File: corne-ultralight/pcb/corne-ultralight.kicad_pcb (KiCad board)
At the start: 2 copper layers, 275.5 x 105.6 mm, 148 parts, among them J2 OLED, J5 Breakaway_Tabs, J7 OLED, SW1 SW_PUSH, SW10 SW_PUSH, SW11 SW_PUSH, SW12 SW_PUSH, SW13 SW_PUSH, SW14 SW_PUSH, SW15 SW_PUSH, SW16 SW_PUSH, SW17 SW_PUSH, SW18 SW_PUSH, SW19 SW_PUSH, SW2 SW_PUSH, SW20 SW_PUSH, SW21 SW_PUSH, SW22 SW_PUSH, SW23 SW_PUSH, SW24 SW_PUSH, SW25 SW_PUSH, SW26 SW_PUSH, SW27 SW_PUSH, SW28 SW_PUSH, SW29 SW_PUSH, SW3 SW_PUSH, SW30 SW_PUSH, SW31 SW_PUSH, SW32 SW_PUSH, SW33 SW_PUSH, SW34 SW_PUSH, SW35 SW_PUSH, SW36 SW_PUSH, SW37 SW_PUSH, SW38 SW_PUSH, SW39 SW_PUSH, SW4 SW_PUSH, SW40 SW_PUSH, SW41 SW_PUSH, SW42 SW_PUSH, SW5 SW_PUSH, SW6 SW_PUSH, SW7 SW_PUSH, SW8 SW_PUSH, SW9 SW_PUSH, U1 ProMicro, U2 ProMicro

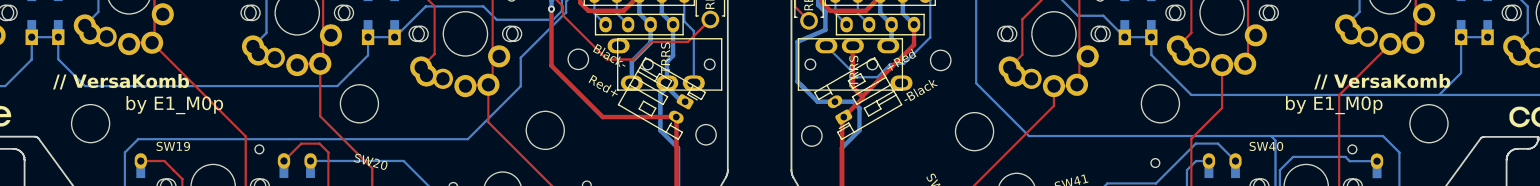
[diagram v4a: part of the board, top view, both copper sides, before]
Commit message: Logo relocated
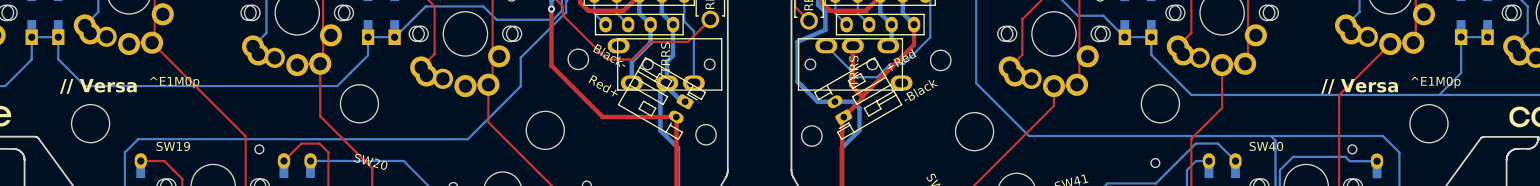
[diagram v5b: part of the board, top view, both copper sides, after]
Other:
- board text added: "// Versa"
- board text added: "^E1M0p"
- board text removed: "// VersaKomb"
- board text removed: "by E1_M0p"
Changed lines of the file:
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@@
 		(layer "Edge.Cuts")
 	)
+	(gr_text "^E1M0p"
+		(at 77.2125 86.945 -0)
+		(layer "B.SilkS")
+		(effects
+			(font
+				(size 1 1)
+				(thickness 0.125)
+			)
+			(justify left mirror)
+		)
+	)
+	(gr_text "^E1M0p"
+		(at 219.484848 86.945 -0)
+		(layer "B.SilkS")
+		(effects
+			(font
+				(size 1 1)
+				(thickness 0.125)
+			)
+			(justify left mirror)
+		)
+	)
 	(gr_text "-Black"
 		(at 141.7125 89.57 -30)
@@
 		)
 	)
+	(gr_text "// Versa"
+		(at 87.216071 87.445 -0)
+		(layer "B.SilkS")
+		(effects
+			(font
+				(size 1.5 1.5)
+				(thickness 0.3)
+				(bold yes)
+			)
+			(justify left mirror)
+		)
+	)
 	(gr_text "ON"
 		(at 141.8525 38.045 180)
@@
 		)
 	)
-	(gr_text "// VersaKomb"
-		(at 87.546428 86.945 -0)
-		(layer "B.SilkS")
-		(effects
-			(font
-				(size 1.5 1.5)
-				(thickness 0.3)
-				(bold yes)
-			)
-			(justify left mirror)
-		)
-	)
 	(gr_text "OFF"
 		(at 168.8525 38.045 180)
@@
 		)
 	)
-	(gr_text "-Black"
-		(at 138.7125 64.945 90)
+	(gr_text "// Versa"
+		(at 229.488419 87.445 -0)
 		(layer "B.SilkS")
 		(effects
 			(font
-				(size 1 1)
-				(thickness 0.15)
+				(size 1.5 1.5)
+				(thickness 0.3)
+				(bold yes)
 			)
 			(justify left mirror)
 		)
 	)
-	(gr_text "by E1_M0p"
-		(at 222.2125 89.445 -0)
+	(gr_text "-Black"
+		(at 138.7125 64.945 90)
 		(layer "B.SilkS")
 		(effects
 			(font
-				(size 1.5 1.5)
-				(thickness 0.1875)
+				(size 1 1)
+				(thickness 0.15)
 			)
 			(justify left mirror)
@@
 		)
 	)
-	(gr_text "// VersaKomb"
-		(at 230.497296 86.945 -0)
-		(layer "B.SilkS")
-		(effects
-			(font
-				(size 1.5 1.5)
-				(thickness 0.3)
-				(bold yes)
-			)
-			(justify left mirror)
-		)
-	)
-	(gr_text "by E1_M0p"
-		(at 90.7125 89.445 -0)
-		(layer "B.SilkS")
-		(effects
-			(font
-				(size 1.5 1.5)
-				(thickness 0.1875)
-			)
-			(justify left mirror)
-		)
-	)
 	(gr_text "Corne Ultralight v2.0 PCB Designed by foostan, mods by petejohanson"
 		(at 191.7125 68.56 0)
@@
 		)
 	)
+	(gr_text "^E1M0p"
+		(at 223.884847 86.945 0)
+		(layer "F.SilkS")
+		(effects
+			(font
+				(size 1 1)
+				(thickness 0.125)
+			)
+			(justify left)
+		)
+	)
 	(gr_text "OFF"
 		(at 171.7125 37.795 180)
@@
 		)
 	)
+	(gr_text "// Versa"
+		(at 213.881276 87.445 0)
+		(layer "F.SilkS")
+		(effects
+			(font
+				(size 1.5 1.5)
+				(thickness 0.3)
+				(bold yes)
+			)
+			(justify left)
+		)
+	)
 	(gr_text "+Red"
 		(at 135.83 59.445 -90)
@@
 		)
 	)
-	(gr_text "// VersaKomb"
-		(at 70.601786 86.945 0)
+	(gr_text "// Versa"
+		(at 71.383929 87.445 0)
 		(layer "F.SilkS")
 		(effects
@@
 		)
 	)
-	(gr_text "by E1_M0p"
-		(at 78.7125 89.445 0)
+	(gr_text "^E1M0p"
+		(at 81.3875 86.945 0)
 		(layer "F.SilkS")
 		(effects
 			(font
-				(size 1.5 1.5)
-				(thickness 0.1875)
+				(size 1 1)
+				(thickness 0.125)
 			)
 			(justify left)
@@
 		)
 	)
-	(gr_text "// VersaKomb"
-		(at 213.099133 86.945 0)
-		(layer "F.SilkS")
-		(effects
-			(font
-				(size 1.5 1.5)
-				(thickness 0.3)
-				(bold yes)
-			)
-			(justify left)
-		)
-	)
 	(gr_text "+Red"
 		(at 170.7125 116.945 30)
@@
 		)
 	)
-	(gr_text "by E1_M0p"
-		(at 209.7125 89.445 0)
-		(layer "F.SilkS")
-		(effects
-			(font
-				(size 1.5 1.5)
-				(thickness 0.1875)
-			)
-			(justify left)
-		)
-	)
 	(gr_text "-Black"
 		(at 169.7125 114.945 30)
@@
 	)
 	(group ""
+		(members "0ffdac26-deab-4092-bf70-1deacd5aef2e" "998406bc-4587-4f5e-a01f-56acd46aa053")
+	)
+	(group ""
+		(members "0d20a1ce-ac43-4072-a8c1-6ed2a3d40657" "204c0979-0e7f-4b7e-9039-b8af16723e6c")
+	)
+	(group ""
 		(members "2187ae59-cf06-4ae2-91b6-236c0a0f70c2" "6999038d-f6d8-4e0f-9d20-872c00953e82"
 			"963028a2-7672-429f-a7cc-4c051f91424c" "9814480d-787a-496e-99a7-91b93430a16f"
@@
 	)
 	(group ""
+		(members "55fb019d-3973-4d45-8622-56472f458ae5" "95f94ae2-a65c-44bb-b344-aae6a263121a")
+	)
+	(group ""
 		(members "013f1f25-df12-4825-a242-8f30f3cd3b16" "5f772bcf-fc59-4ca1-a4e6-d1eedcd91c5c")
 	)
@@
 	)
 	(group ""
+		(members "1c0b1fae-bb3e-4696-8439-dd348b1b6155" "2835c844-1c04-458d-9ca5-06f73f505be4")
+	)
+	(group ""

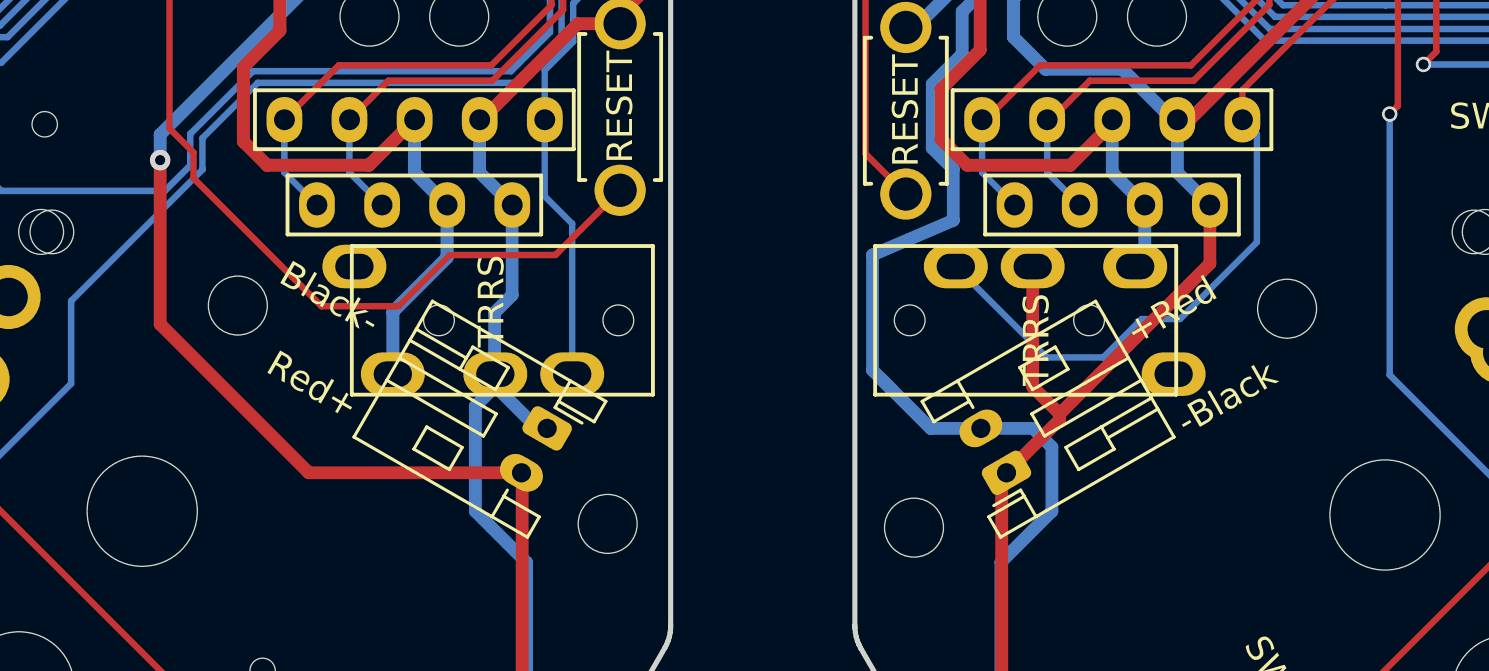
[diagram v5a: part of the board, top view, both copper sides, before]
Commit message: Two small cable holes at the bottom edge of the visor
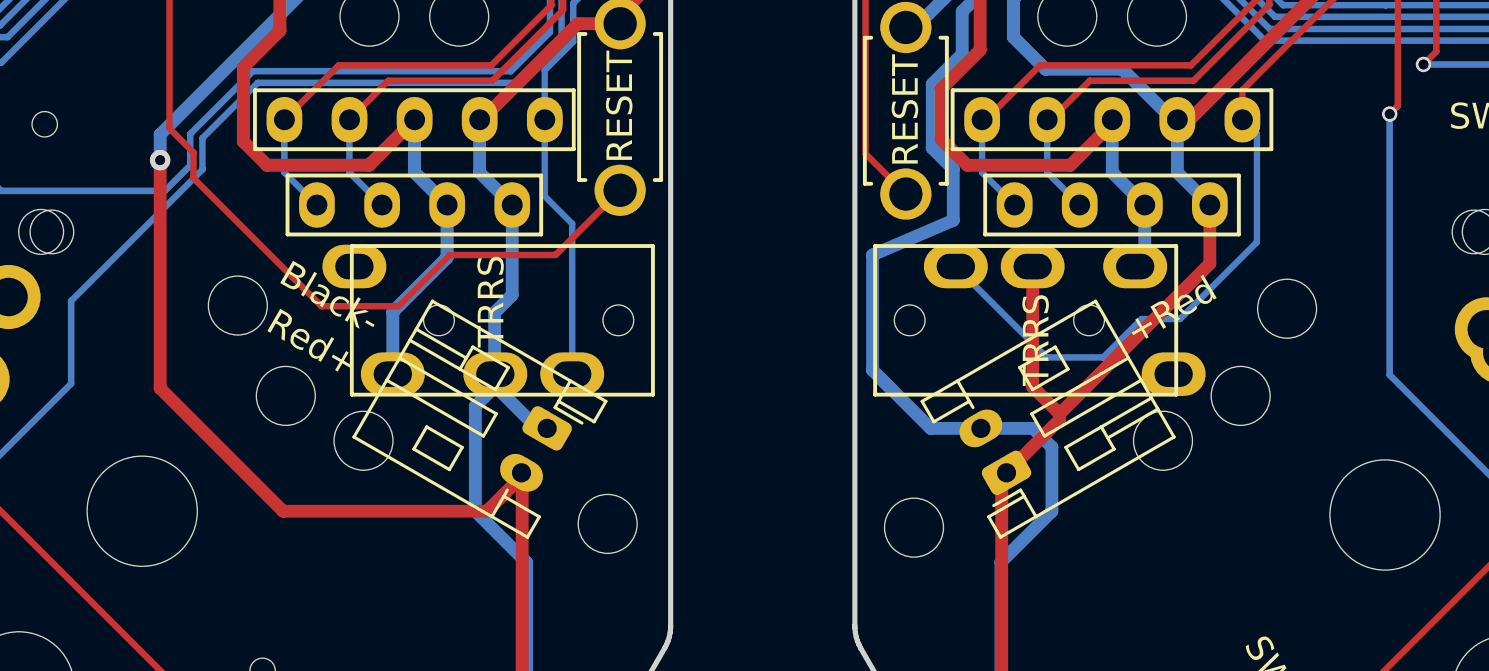
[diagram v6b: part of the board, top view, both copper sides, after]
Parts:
- added Ref**: Val**, kbd:thread_m2, F.Cu at (131.8, 87.9)
- added Ref**: Val**, kbd:thread_m2, F.Cu at (134.8, 89.7)
- added Ref**: Val**, kbd:thread_m2, F.Cu at (166.0, 89.7)
- added Ref**: Val**, kbd:thread_m2, F.Cu at (169.1, 87.9)
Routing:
- net Net-(BATJ1-Pin_2): track 97.3 -> 99.9 mm

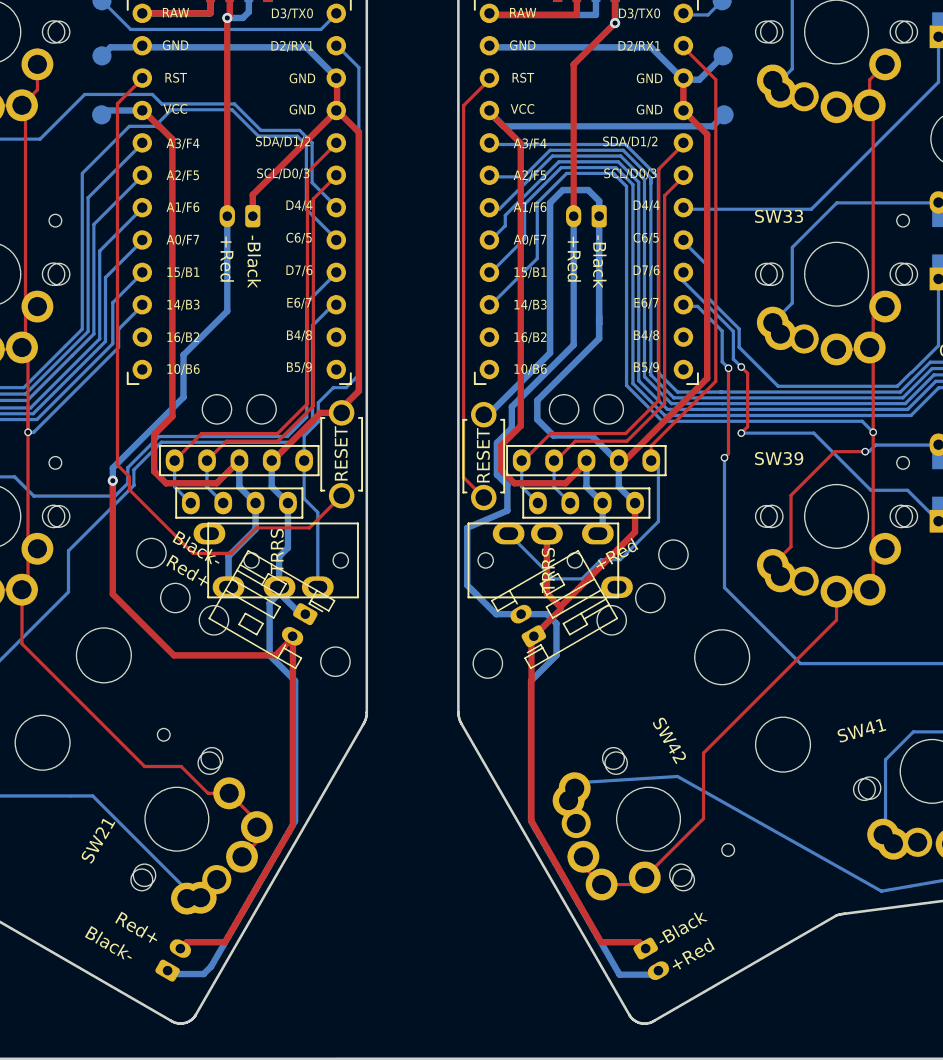
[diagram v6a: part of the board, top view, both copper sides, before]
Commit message: Improved cable holes
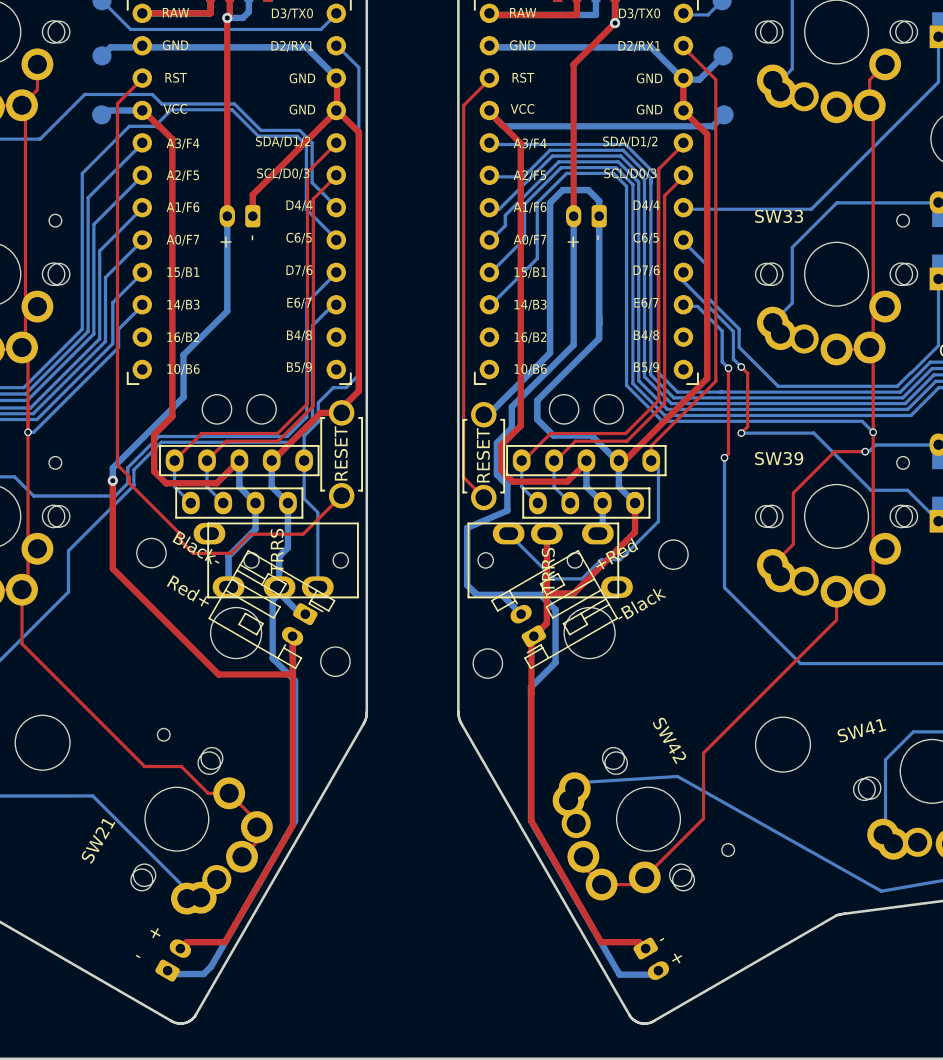
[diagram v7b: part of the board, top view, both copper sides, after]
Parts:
- removed the Ref** at (131.8, 87.9)
- removed the Ref** at (126.2, 92.4)
- removed the Ref** at (174.7, 92.6)
- removed the Ref** at (134.8, 89.7)
- removed the Ref** at (166.0, 89.7)
- removed the Ref** at (169.1, 87.9)
- added Ref**: Val**, kbd:spacer_m2, B.Cu at (137.3, 90.7)
- added Ref**: Val**, kbd:spacer_m2, B.Cu at (164.1, 91.9)
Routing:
- net Net-(BATJ4-Pin_2): track 97.6 -> 100.8 mm
- net Net-(BATJ1-Pin_2): track 99.9 -> 101.6 mm
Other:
- board text added: "+"
- board text added: "-"

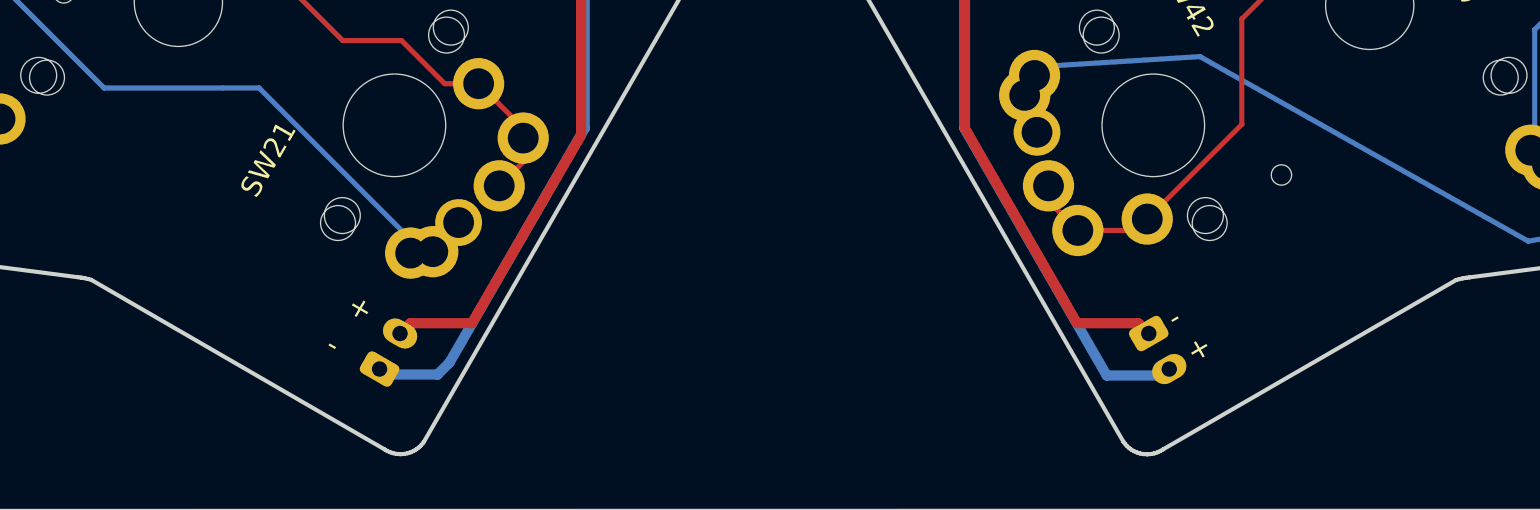
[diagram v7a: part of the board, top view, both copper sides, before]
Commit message: Bottom JST moved
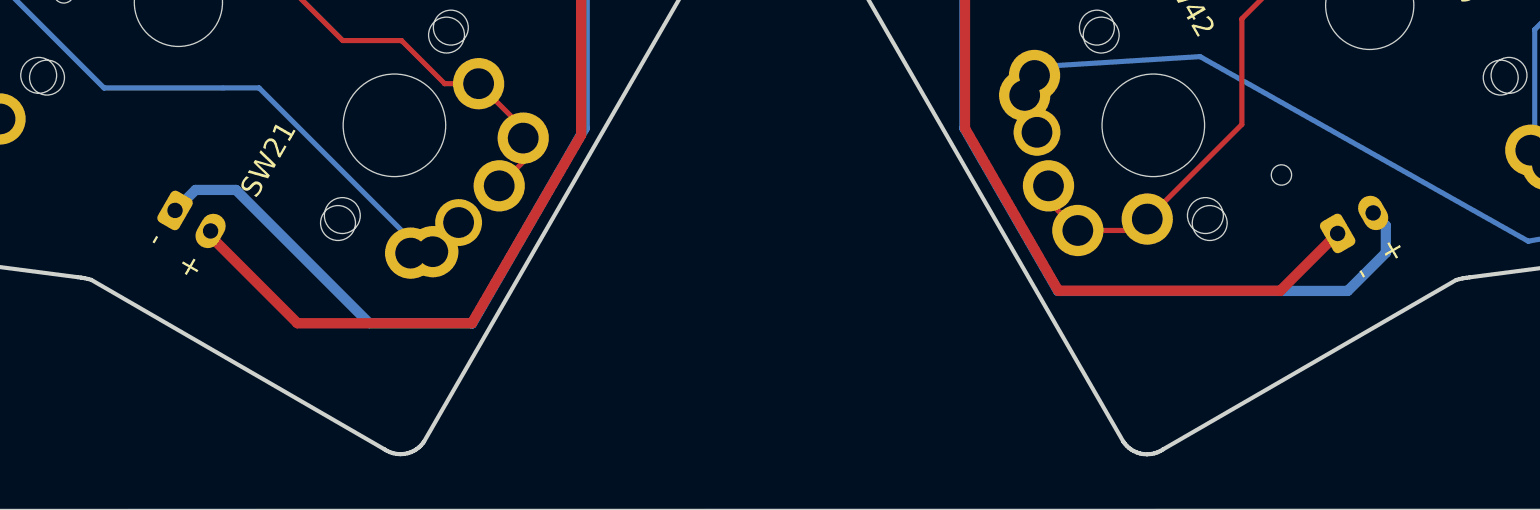
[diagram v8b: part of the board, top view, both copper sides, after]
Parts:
- moved BATJ7 12.6 mm to (121.2, 109.4), turned to -30 degrees
- moved BATJ8 10.4 mm to (177.9, 110.6), turned to 30 degrees
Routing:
- net GND: track 115.6 -> 127.3 mm
- net Net-(BATJ1-Pin_2): track 101.6 -> 112.7 mm
- net Net-(BATJ4-Pin_2): track 100.8 -> 111.6 mm
- net GNDA: track 158.0 -> 167.2 mm
